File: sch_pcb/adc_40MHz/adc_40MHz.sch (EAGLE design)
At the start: 72 parts, among them IC1 AD9235BC, IC2 LT6600-15, IC3 LTC6254XMS, IC4 SN74LVC2G14DBV, IC5 LT1521XST, IC6 SN74LVC2G14DBV, X1 SMA-142-0701-851/861, X2 SMA-142-0701-851/861

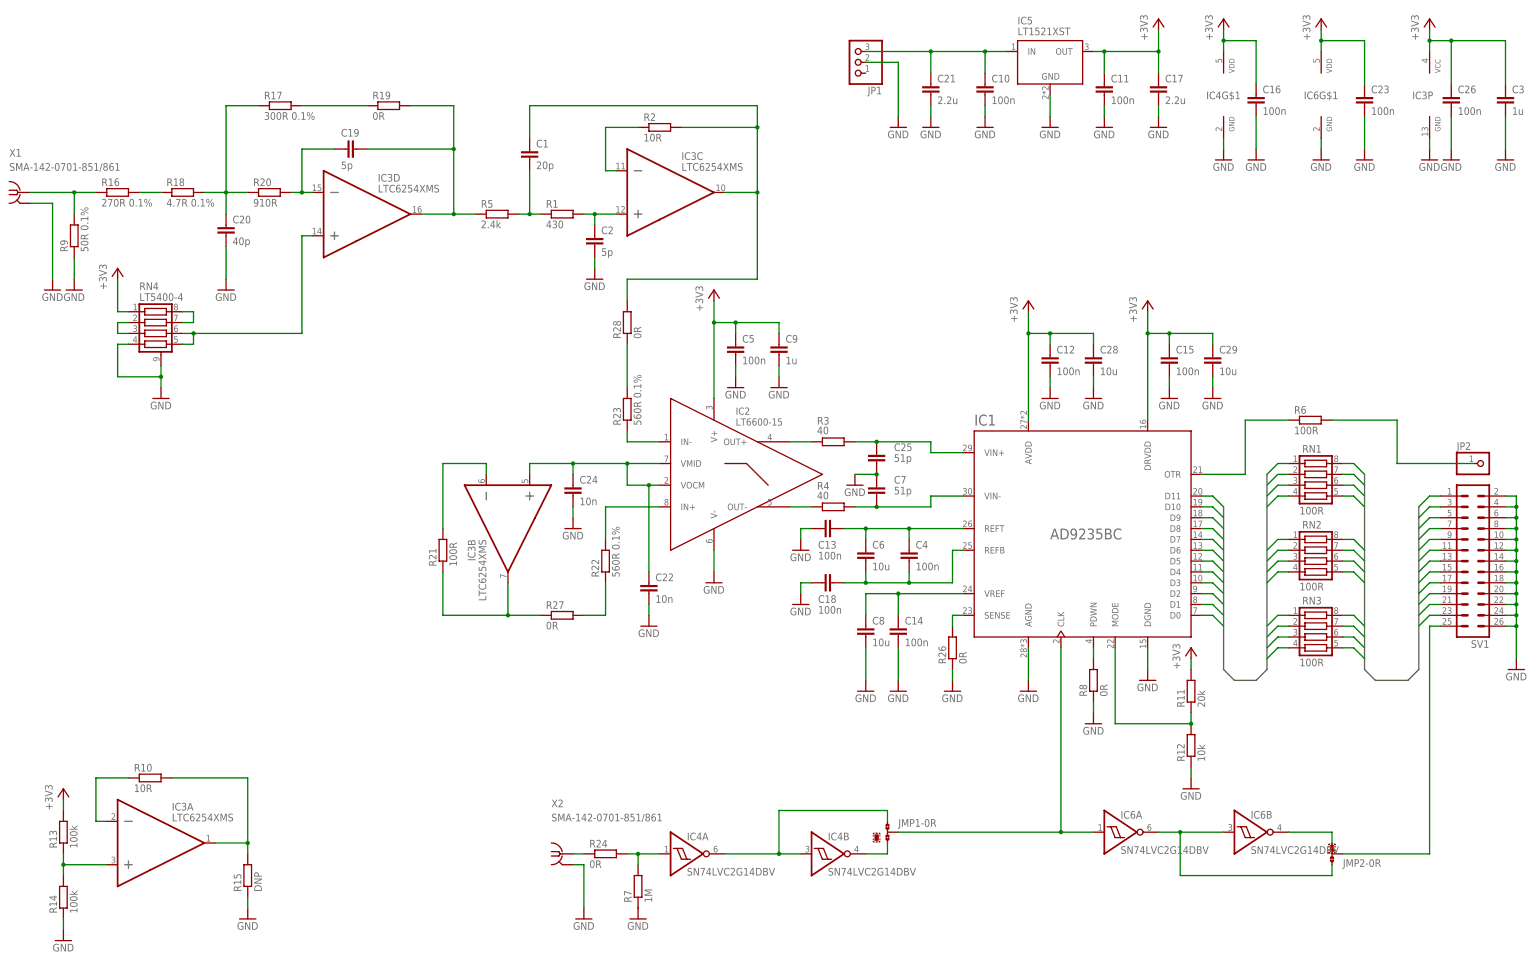
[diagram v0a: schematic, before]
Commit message: Usunięto niepotrzebne rezystory, aby ułatwić projekt ścieżek. Gotowa płytka
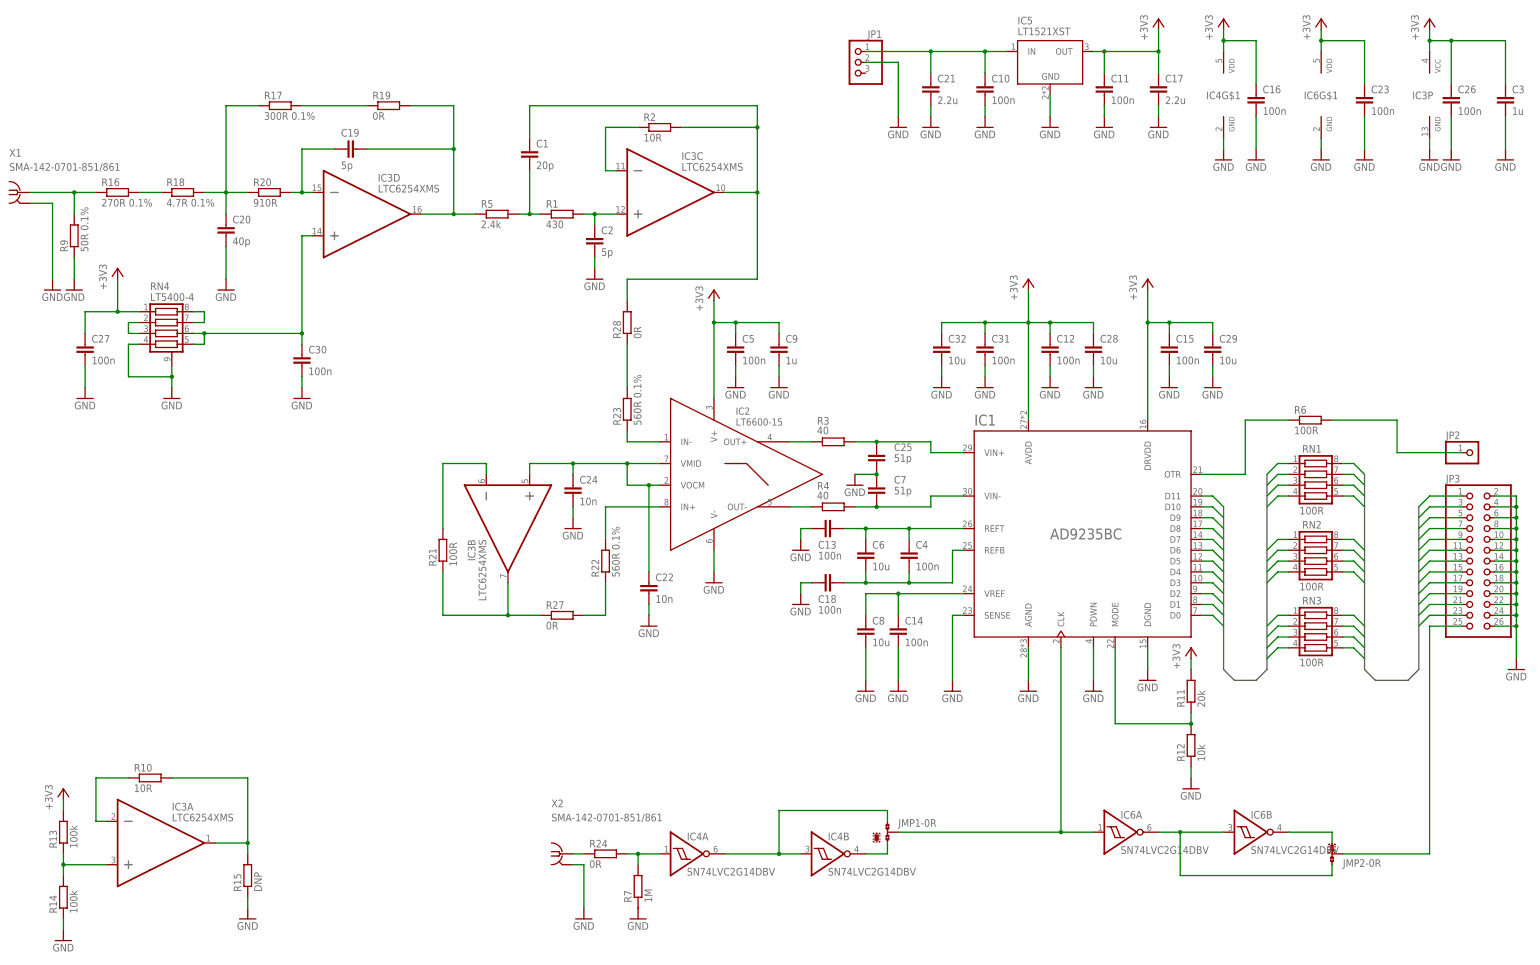
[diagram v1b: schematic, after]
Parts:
- removed R26, R8: 0R, rcl:R-EU_R0603
- removed SV1: (no value), con-harting-ml:ML26
- added C27, C30, C31: 100n, resistor:C-EUC0603K
- added C32: 10u, rcl:C-EUC1206
- added JP3: (no value), moj_pinhead:PINHD-2X13
- JP1: device pinhead:PINHD-1X3/90 -> moj_pinhead:PINHD-1X3
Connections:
- removed net N$35: IC1.SENSE, R26.2
- removed net N$9: IC1.PDWN, R8.2
- net +3V3: now also C27.1, C31.1, C32.1
- net CLK: now also JP3.25; no longer SV1.25
- net DAC_D0: now also JP3.23; no longer SV1.23
- net DAC_D1: now also JP3.21; no longer SV1.21
- net DAC_D10: now also JP3.3; no longer SV1.3
- net DAC_D11: now also JP3.1; no longer SV1.1
- net DAC_D2: now also JP3.19; no longer SV1.19
- net DAC_D3: now also JP3.17; no longer SV1.17
- net DAC_D4: now also JP3.15; no longer SV1.15
- net DAC_D5: now also JP3.13; no longer SV1.13
- net DAC_D6: now also JP3.11; no longer SV1.11
- net DAC_D7: now also JP3.9; no longer SV1.9
- net DAC_D8: now also JP3.7; no longer SV1.7
- net DAC_D9: now also JP3.5; no longer SV1.5
- net GND: now also C27.2, C30.2, C31.2, C32.2, IC1.PDWN, IC1.SENSE, JP3.10, JP3.12, JP3.14, JP3.16, JP3.18, JP3.2, JP3.20, JP3.22, JP3.24, JP3.26, JP3.4, JP3.6, JP3.8; no longer R26.1, R8.1, SV1.10, SV1.12, SV1.14, SV1.16, SV1.18, SV1.2, SV1.20, SV1.22, SV1.24, SV1.26, SV1.4, SV1.6, SV1.8
- net N$24: now also C30.1
- net VIN: now also JP1.1; no longer JP1.3
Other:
- moved on the sheet: C12, C15, C28, C29, JP1, JP2, RN4

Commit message: Niewielkie poprawki - dodano połączenie masy przy ADC
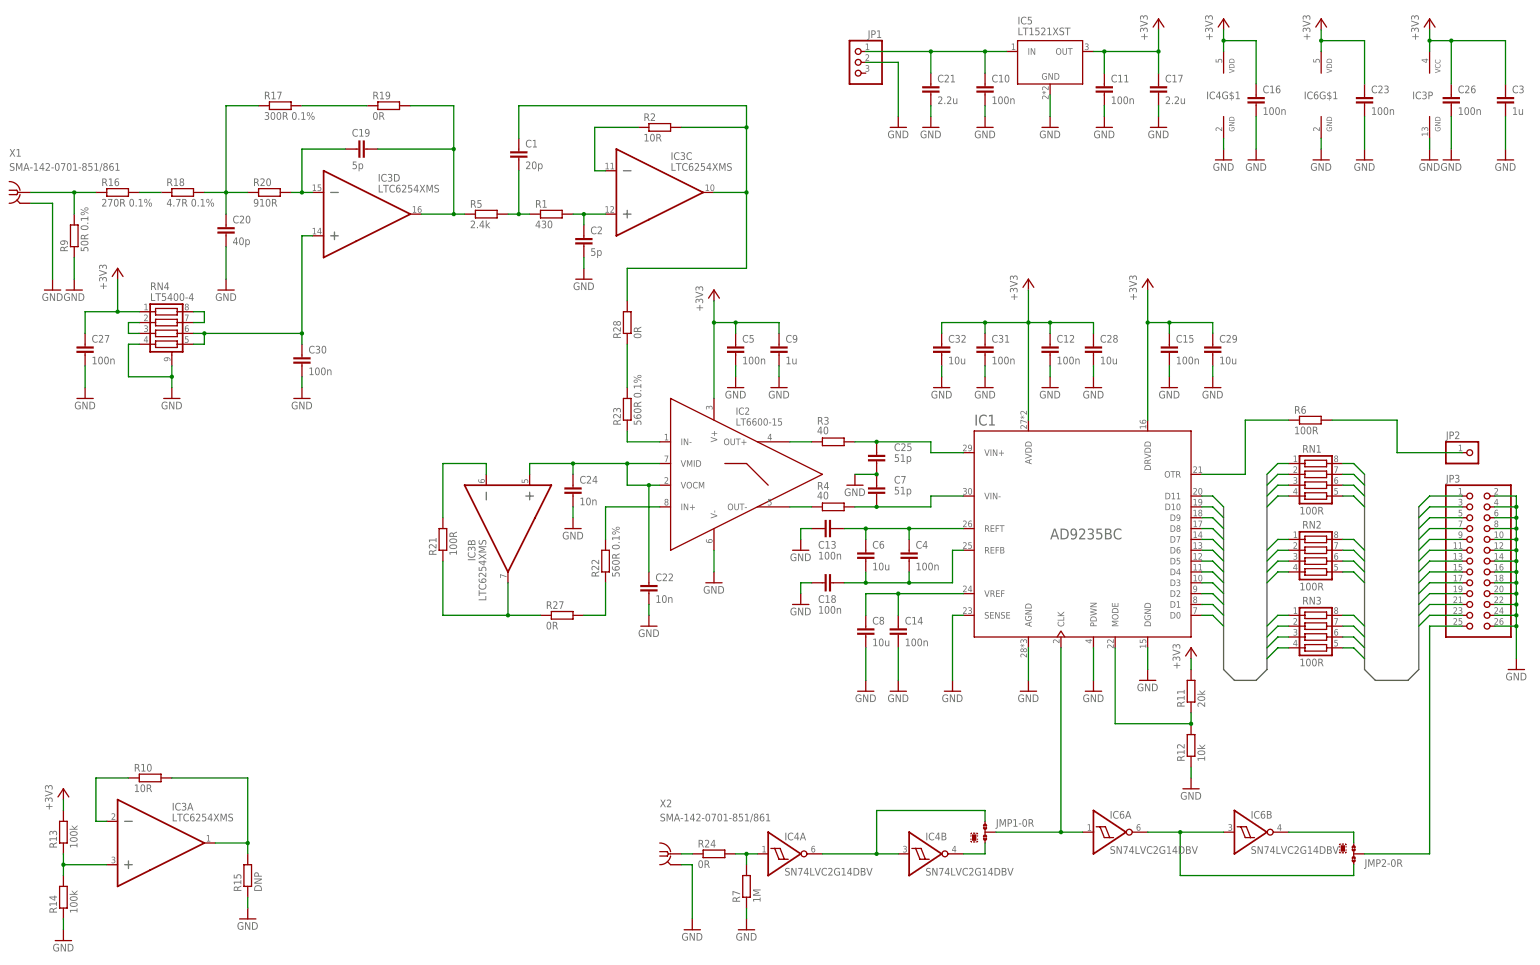
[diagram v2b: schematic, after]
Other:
- moved on the sheet: C1, C19, C2, IC3C, IC4A, IC4B, IC6A, JMP1-0R, JMP2-0R, R1, R21, R24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

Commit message: Dodano BOM, poprawiono wartości niektórych rezystancji
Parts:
- R1: value 430 -> 430R
- R3, R4: value 40 -> 40R
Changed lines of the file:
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@@
 <parts>
 <part name="FRAME1" library="frames" deviceset="A3L-LOC" device=""/>
-<part name="R3" library="rcl" deviceset="R-EU_" device="R0603" value="40"/>
-<part name="R4" library="rcl" deviceset="R-EU_" device="R0603" value="40"/>
+<part name="R3" library="rcl" deviceset="R-EU_" device="R0603" value="40R"/>
+<part name="R4" library="rcl" deviceset="R-EU_" device="R0603" value="40R"/>
 <part name="R5" library="rcl" deviceset="R-EU_" device="R0603" value="2.4k"/>
 <part name="C5" library="resistor" deviceset="C-EU" device="C0603K" value="100n"/>
@@
 <part name="R11" library="rcl" deviceset="R-EU_" device="R0603" value="20k"/>
 <part name="R12" library="rcl" deviceset="R-EU_" device="R0603" value="10k"/>
-<part name="R1" library="rcl" deviceset="R-EU_" device="R0603" value="430"/>
+<part name="R1" library="rcl" deviceset="R-EU_" device="R0603" value="430R"/>
 <part name="C1" library="resistor" deviceset="C-EU" device="C0603K" value="20p"/>
 <part name="C2" library="resistor" deviceset="C-EU" device="C0603K" value="5p"/>
